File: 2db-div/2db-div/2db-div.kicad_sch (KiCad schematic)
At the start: 34 parts, among them J1001 Conn_01x02, J1002 From R2, J1003 Conn_01x02, J1004 Conn_Coaxial, SW1001 SW_SPDT, SW1002 Video, U1001 MC1458

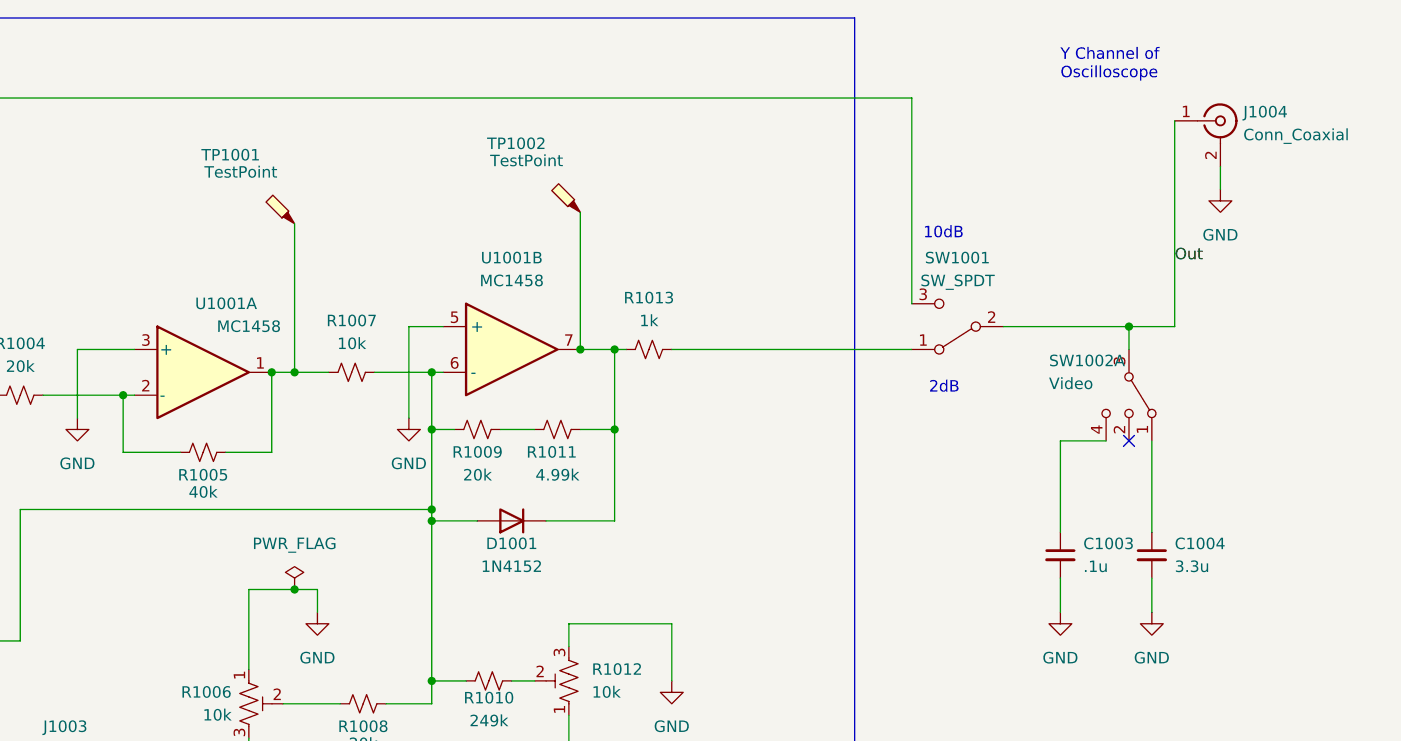
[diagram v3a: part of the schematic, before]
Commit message: BOM for 2db-div
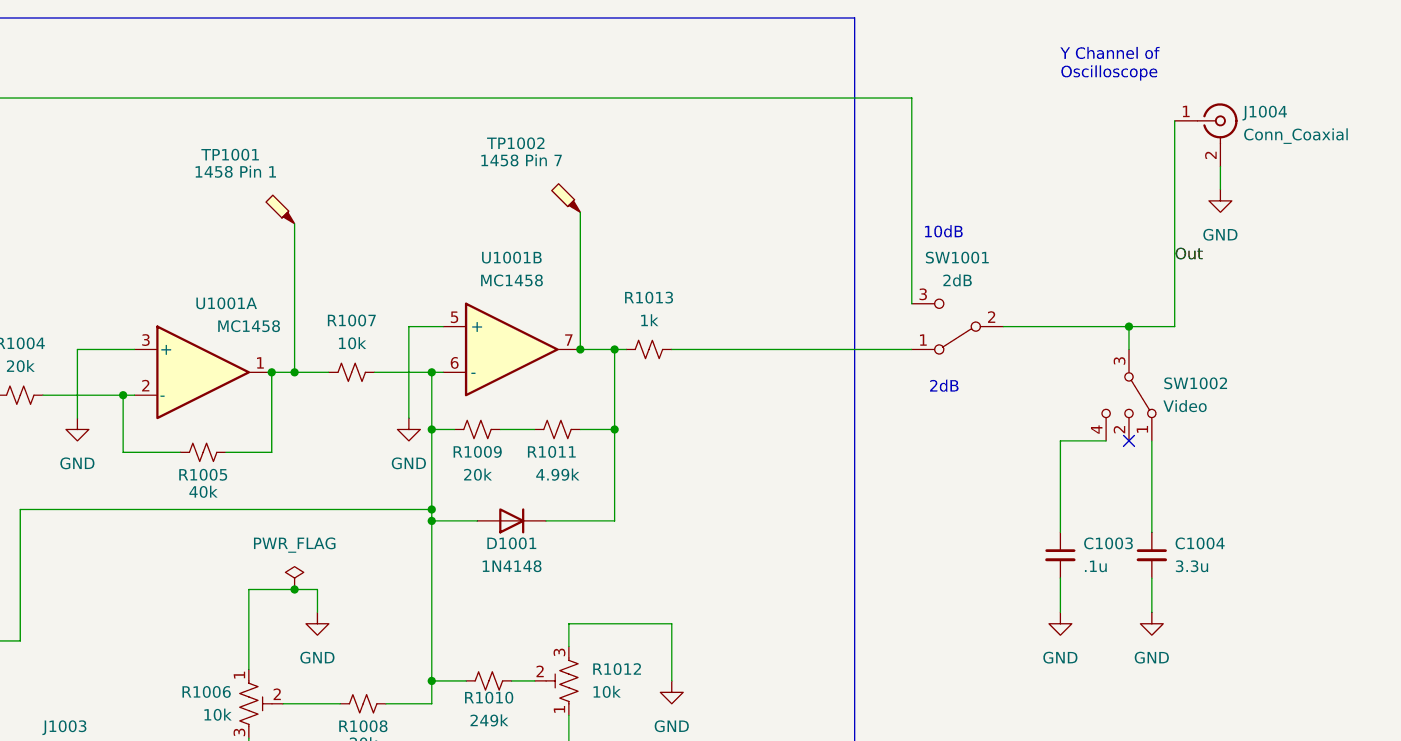
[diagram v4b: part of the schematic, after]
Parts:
- removed SW1002: Video, symbol Switch:SW_DP3T
- added SW1002: Video, symbol Switch:SW_SP3T
- D1001: value 1N4152 -> 1N4148
- SW1001: value SW_SPDT -> 2dB
- TP1001: value TestPoint -> 1458 Pin 1
- TP1002: value TestPoint -> 1458 Pin 7
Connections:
- net Out: now also SW1002.3
- net at C1004.1: now also SW1002.1
- net at C1003.1: now also SW1002.4
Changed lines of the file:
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@@
       (effects (font (size 1.27 1.27)) hide)
     )
-    (property "Datasheet" "" (id 3) (at 132.08 82.55 0))
+    (property "Datasheet" "https://www.ti.com/lit/ds/symlink/mc1458.pdf?HQS=dis-dk-null-digikeymode-dsf-pf-null-wwe&ts=1661113731735&ref_url=https%253A%252F%252Fwww.ti.com%252Fgeneral%252Fdocs%252Fsuppproductinfo.tsp%253FdistId%253D10%2526gotoUrl%253Dhttps%253A%252F%252Fwww.ti.com%252Flit%252Fgpn%252Fmc1458" (id 3) (at 132.08 82.55 0)
+      (effects (font (size 1.27 1.27)) hide)
+    )
     (property "Spice_Primitive" "X" (id 4) (at 132.08 82.55 0)
       (effects (font (size 1.27 1.27)) hide)
@@
     (pin "1")
   )
-  (symbol (lib_id "Switch:SW_DP3T") (at 227.33 85.09 270) (unit 1)
-    (in_bom yes) (on_board no)
-    (property "Reference" "SW1002" (id 0) (at 218.44 81.28 90)
-      (effects (font (size 1.27 1.27)) (justify left))
-    )
-    (property "Value" "Video" (id 1) (at 218.44 83.82 90)
+  (symbol (lib_id "power:GND") (at 49.53 193.04 0) (unit 1)
+    (in_bom yes) (on_board yes) (fields_autoplaced)
+    (property "Reference" "#PWR01002" (id 0) (at 49.53 199.39 0)
+      (effects (font (size 1.27 1.27)) hide)
+    )
+    (property "Value" "GND" (id 1) (at 49.53 198.12 0))
+    (property "Footprint" "" (id 2) (at 49.53 193.04 0)
+      (effects (font (size 1.27 1.27)) hide)
+    )
+    (property "Datasheet" "" (id 3) (at 49.53 193.04 0)
+      (effects (font (size 1.27 1.27)) hide)
+    )
+    (pin "1")
+  )
+  (symbol (lib_id "Switch:SW_SP3T") (at 227.33 85.09 270) (unit 1)
+    (in_bom yes) (on_board no) (fields_autoplaced)
+    (property "Reference" "SW1002" (id 0) (at 231.14 83.8199 90)
+      (effects (font (size 1.27 1.27)) (justify left))
+    )
+    (property "Value" "Video" (id 1) (at 231.14 86.3599 90)
       (effects (font (size 1.27 1.27)) (justify left))
     )
@@
     )
     (property "Datasheet" "~" (id 3) (at 231.775 69.215 0)
-      (effects (font (size 1.27 1.27)) hide)
-    )
-    (property "Spice_Primitive" "R" (id 4) (at 227.33 85.09 0)
-      (effects (font (size 1.27 1.27)) hide)
-    )
-    (property "Spice_Netlist_Enabled" "N" (id 5) (at 227.33 85.09 0)
       (effects (font (size 1.27 1.27)) hide)
     )
@@
     (pin "3")
     (pin "4")
-    (pin "5")
-    (pin "6")
-    (pin "7")
-    (pin "8")
-  )
-  (symbol (lib_id "power:GND") (at 49.53 193.04 0) (unit 1)
-    (in_bom yes) (on_board yes) (fields_autoplaced)
-    (property "Reference" "#PWR01002" (id 0) (at 49.53 199.39 0)
-      (effects (font (size 1.27 1.27)) hide)
-    )
-    (property "Value" "GND" (id 1) (at 49.53 198.12 0))
-    (property "Footprint" "" (id 2) (at 49.53 193.04 0)
-      (effects (font (size 1.27 1.27)) hide)
-    )
-    (property "Datasheet" "" (id 3) (at 49.53 193.04 0)
-      (effects (font (size 1.27 1.27)) hide)
-    )
-    (pin "1")
   )
   (symbol (lib_id "power:GND") (at 57.15 101.6 0) (unit 1)
@@
     (in_bom yes) (on_board no) (fields_autoplaced)
     (property "Reference" "SW1001" (id 0) (at 208.28 69.85 0))
-    (property "Value" "SW_SPDT" (id 1) (at 208.28 72.39 0))
+    (property "Value" "2dB" (id 1) (at 208.28 72.39 0))
     (property "Footprint" "" (id 2) (at 208.28 77.47 0)
       (effects (font (size 1.27 1.27)) hide)
@@
       (effects (font (size 1.27 1.27)) hide)
     )
-    (property "Datasheet" "~" (id 3) (at 78.74 123.19 0)
+    (property "Datasheet" "https://www.ti.com/lit/ds/symlink/mc1458.pdf?HQS=dis-dk-null-digikeymode-dsf-pf-null-wwe&ts=1661113731735&ref_url=https%253A%252F%252Fwww.ti.com%252Fgeneral%252Fdocs%252Fsuppproductinfo.tsp%253FdistId%253D10%2526gotoUrl%253Dhttps%253A%252F%252Fwww.ti.com%252Flit%252Fgpn%252Fmc1458" (id 3) (at 78.74 123.19 0)
       (effects (font (size 1.27 1.27)) hide)
     )
@@
       (effects (font (size 1.27 1.27)) (justify left))
     )
-    (property "Value" "TestPoint" (id 1) (at 164.465 59.055 0)
+    (property "Value" "1458 Pin 7" (id 1) (at 164.465 59.055 0)
       (effects (font (size 1.27 1.27)) (justify left))
     )
@@
       (effects (font (size 1.27 1.27)) (justify left))
     )
-    (property "Value" "TestPoint" (id 1) (at 132.715 60.325 0)
+    (property "Value" "1458 Pin 1" (id 1) (at 132.715 60.325 0)
       (effects (font (size 1.27 1.27)) (justify left))
     )
@@
     (in_bom yes) (on_board yes)
     (property "Reference" "D1001" (id 0) (at 158.75 101.6 0))
-    (property "Value" "1N4152" (id 1) (at 158.75 104.14 0))
+    (property "Value" "1N4148" (id 1) (at 158.75 104.14 0))
     (property "Footprint" "Diode_THT:D_DO-35_SOD27_P7.62mm_Horizontal" (id 2) (at 160.02 101.6 0)
       (effects (font (size 1.27 1.27)) hide)
@@
       (effects (font (size 1.27 1.27)) hide)
     )
-    (property "Datasheet" "~" (id 3) (at 158.75 80.01 0)
+    (property "Datasheet" "https://www.ti.com/lit/ds/symlink/mc1458.pdf?HQS=dis-dk-null-digikeymode-dsf-pf-null-wwe&ts=1661113731735&ref_url=https%253A%252F%252Fwww.ti.com%252Fgeneral%252Fdocs%252Fsuppproductinfo.tsp%253FdistId%253D10%2526gotoUrl%253Dhttps%253A%252F%252Fwww.ti.com%252Flit%252Fgpn%252Fmc1458" (id 3) (at 158.75 80.01 0)
       (effects (font (size 1.27 1.27)) hide)
     )
@@
     )
     (path "/d93477ae-5620-45e8-ad77-f7159e7b54ac"
-      (reference "D1001") (unit 1) (value "1N4152") (footprint "Diode_THT:D_DO-35_SOD27_P7.62mm_Horizontal")
+      (reference "D1001") (unit 1) (value "1N4148") (footprint "Diode_THT:D_DO-35_SOD27_P7.62mm_Horizontal")
     )
     (path "/39de73f6-b9de-4b63-8f42-aee5d12d3f40"
@@
     )
     (path "/7635f8f1-e32f-4bba-9fa7-adca3b4a9d43"
-      (reference "SW1001") (unit 1) (value "SW_SPDT") (footprint "")
-    )
-    (path "/1cab3287-f614-4c42-a22f-d78d04c3f6d0"
+      (reference "SW1001") (unit 1) (value "2dB") (footprint "")
+    )
+    (path "/268e017f-79dc-4e8c-ba2c-4bb52ba02a9d"
       (reference "SW1002") (unit 1) (value "Video") (footprint "")
     )
     (path "/b72f73df-8f47-4328-948e-122e87b26001"
-      (reference "TP1001") (unit 1) (value "TestPoint") (footprint "TestPoint:TestPoint_Pad_1.0x1.0mm")
+      (reference "TP1001") (unit 1) (value "1458 Pin 1") (footprint "TestPoint:TestPoint_Pad_1.0x1.0mm")
     )
     (path "/b1b40c84-9a02-4510-86b5-29948f09db79"
-      (reference "TP1002") (unit 1) (value "TestPoint") (footprint "TestPoint:TestPoint_Pad_1.0x1.0mm")
+      (reference "TP1002") (unit 1) (value "1458 Pin 7") (footprint "TestPoint:TestPoint_Pad_1.0x1.0mm")
     )
     (path "/15fa4751-8172-4686-95f4-602bee0fff9e"

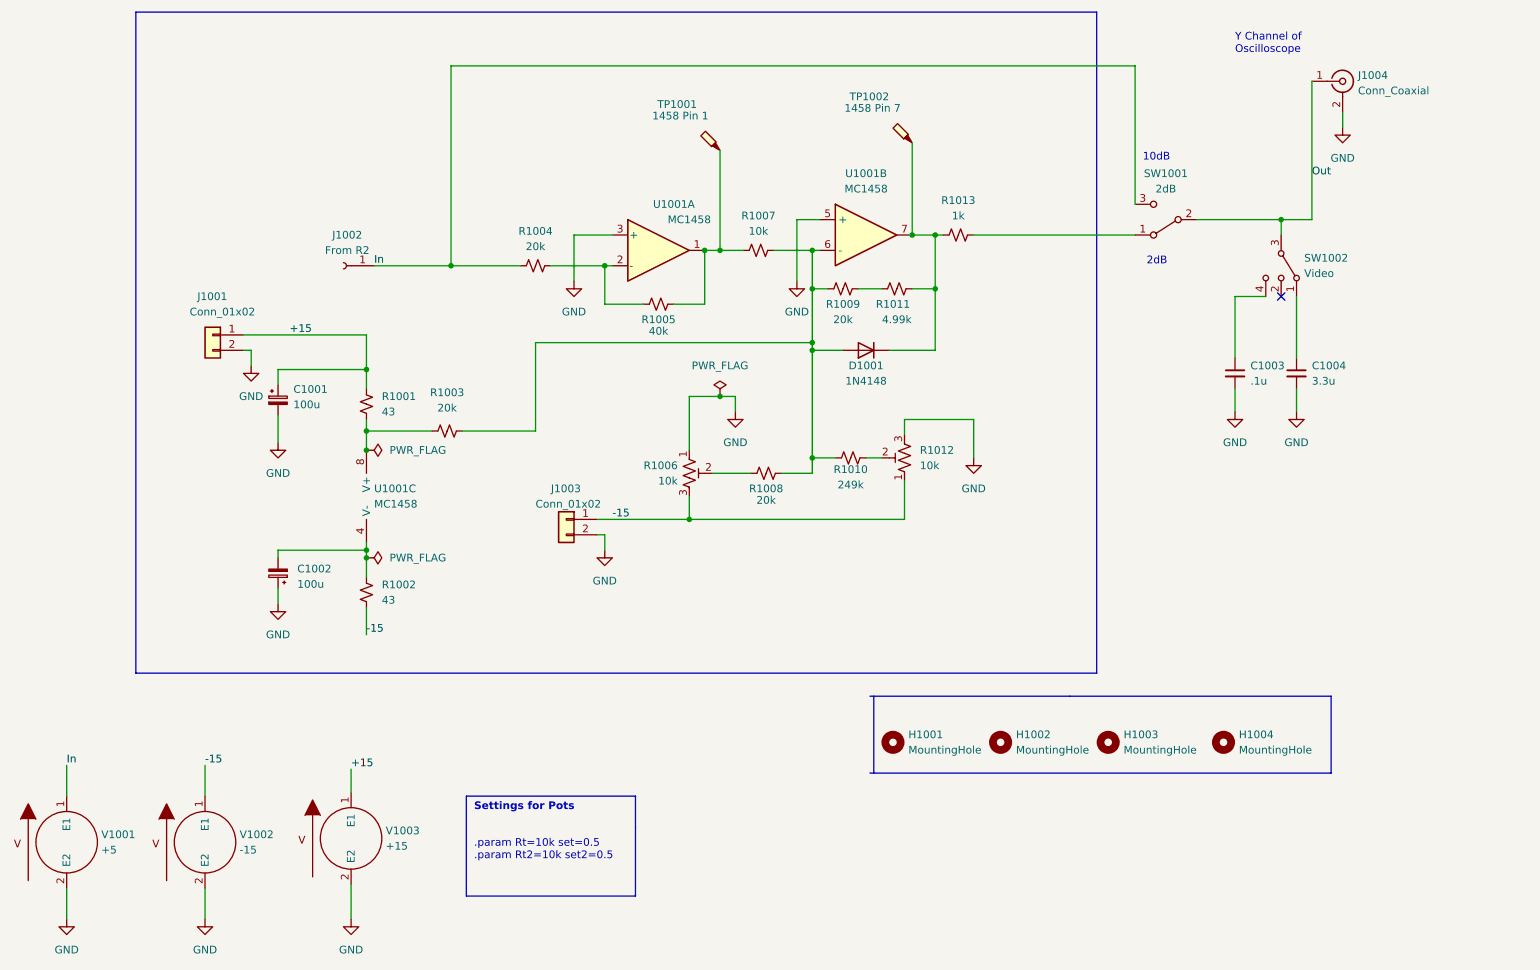
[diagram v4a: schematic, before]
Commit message: Hierarchical schematic updates
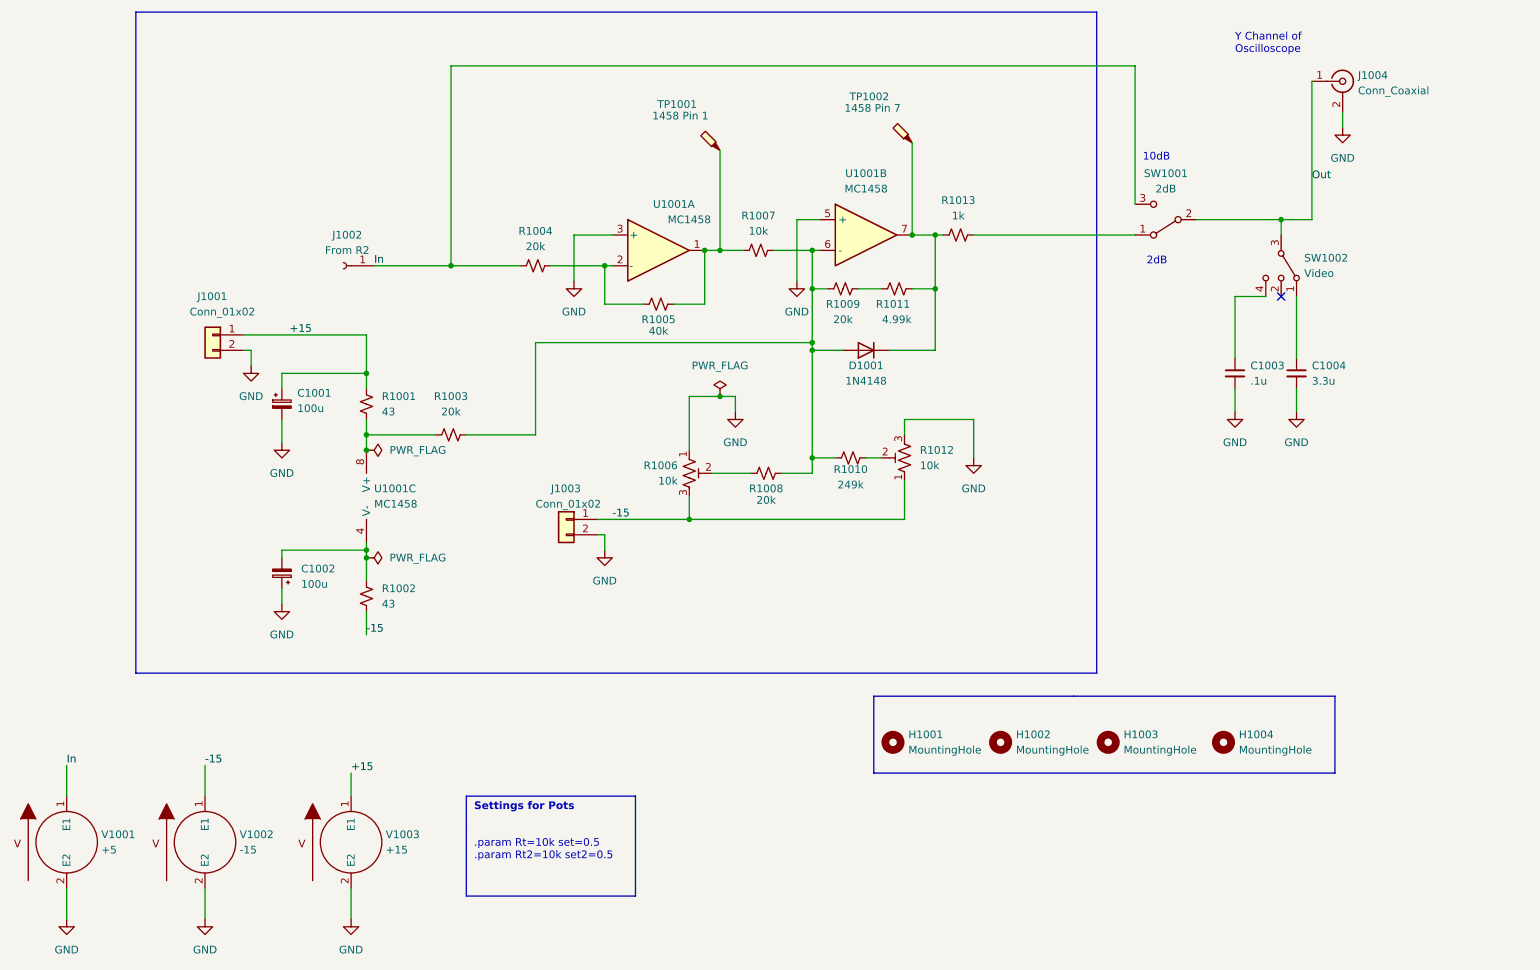
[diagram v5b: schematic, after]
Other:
- moved on the sheet: C1001, C1002, R1002, R1003, V1003

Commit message: minor changes for spice
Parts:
- H1001, H1002, H1003, H1004, SW1002: Spice_Netlist_Enabled (none) -> N; Spice_Primitive (none) -> R
- J1002: Spice_Model (none) -> From R2; Spice_Netlist_Enabled (none) -> N; Spice_Primitive (none) -> J
- SW1001: Spice_Model (none) -> 2dB
- U1001: Spice_Lib_File 2db-div-spice\MC1458-dual.lib -> 2db-div-spice\LM358-dual.lib; Spice_Model MC1458_ti -> LM358c; Spice_Netlist_Enabled Y -> N
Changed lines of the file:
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@@
+      (effects (font (size 1.27 1.27)) hide)
+    )
+    (property "Spice_Primitive" "R" (id 4) (at 180.975 163.83 0)
+      (effects (font (size 1.27 1.27)) hide)
+    )
+    (property "Spice_Netlist_Enabled" "N" (id 5) (at 180.975 163.83 0)
       (effects (font (size 1.27 1.27)) hide)
     )
@@
       (effects (font (size 1.27 1.27)) hide)
     )
-    (property "Spice_Model" "MC1458_ti" (id 5) (at 132.08 82.55 0)
-      (effects (font (size 1.27 1.27)) hide)
-    )
-    (property "Spice_Netlist_Enabled" "Y" (id 6) (at 132.08 82.55 0)
-      (effects (font (size 1.27 1.27)) hide)
-    )
-    (property "Spice_Lib_File" "2db-div-spice\\MC1458-dual.lib" (id 7) (at 132.08 82.55 0)
+    (property "Spice_Model" "LM358c" (id 5) (at 132.08 82.55 0)
+      (effects (font (size 1.27 1.27)) hide)
+    )
+    (property "Spice_Netlist_Enabled" "N" (id 6) (at 132.08 82.55 0)
+      (effects (font (size 1.27 1.27)) hide)
+    )
+    (property "Spice_Lib_File" "2db-div-spice\\LM358-dual.lib" (id 7) (at 132.08 82.55 0)
       (effects (font (size 1.27 1.27)) hide)
     )
@@
       (effects (font (size 1.27 1.27)) hide)
     )
+    (property "Spice_Primitive" "R" (id 4) (at 227.33 85.09 0)
+      (effects (font (size 1.27 1.27)) hide)
+    )
+    (property "Spice_Netlist_Enabled" "N" (id 5) (at 227.33 85.09 0)
+      (effects (font (size 1.27 1.27)) hide)
+    )
     (pin "1")
     (pin "2")
@@
       (effects (font (size 1.27 1.27)) hide)
     )
+    (property "Spice_Primitive" "R" (id 4) (at 217.805 163.83 0)
+      (effects (font (size 1.27 1.27)) hide)
+    )
+    (property "Spice_Netlist_Enabled" "N" (id 5) (at 217.805 163.83 0)
+      (effects (font (size 1.27 1.27)) hide)
+    )
   )
   (symbol (lib_id "Mechanical:MountingHole") (at 163.195 163.83 0) (unit 1)
@@
     )
     (property "Datasheet" "~" (id 3) (at 163.195 163.83 0)
+      (effects (font (size 1.27 1.27)) hide)
+    )
+    (property "Spice_Primitive" "R" (id 4) (at 163.195 163.83 0)
+      (effects (font (size 1.27 1.27)) hide)
+    )
+    (property "Spice_Netlist_Enabled" "N" (id 5) (at 163.195 163.83 0)
       (effects (font (size 1.27 1.27)) hide)
     )
@@
     )
     (property "Datasheet" "~" (id 3) (at 198.755 163.83 0)
+      (effects (font (size 1.27 1.27)) hide)
+    )
+    (property "Spice_Primitive" "R" (id 4) (at 198.755 163.83 0)
+      (effects (font (size 1.27 1.27)) hide)
+    )
+    (property "Spice_Netlist_Enabled" "N" (id 5) (at 198.755 163.83 0)
       (effects (font (size 1.27 1.27)) hide)
     )
@@
       (effects (font (size 1.27 1.27)) hide)
     )
+    (property "Spice_Model" "2dB" (id 6) (at 208.28 77.47 0)
+      (effects (font (size 1.27 1.27)) hide)
+    )
     (pin "1")
     (pin "2")
@@
       (effects (font (size 1.27 1.27)) hide)
     )
-    (property "Spice_Model" "MC1458_ti" (id 5) (at 155.575 80.01 0)
-      (effects (font (size 1.27 1.27)) hide)
-    )
-    (property "Spice_Netlist_Enabled" "Y" (id 6) (at 155.575 80.01 0)
-      (effects (font (size 1.27 1.27)) hide)
-    )
-    (property "Spice_Lib_File" "2db-div-spice\\MC1458-dual.lib" (id 7) (at 155.575 80.01 0)
+    (property "Spice_Model" "LM358c" (id 5) (at 155.575 80.01 0)
+      (effects (font (size 1.27 1.27)) hide)
+    )
+    (property "Spice_Netlist_Enabled" "N" (id 6) (at 155.575 80.01 0)
+      (effects (font (size 1.27 1.27)) hide)
+    )
+    (property "Spice_Lib_File" "2db-div-spice\\LM358-dual.lib" (id 7) (at 155.575 80.01 0)
       (effects (font (size 1.27 1.27)) hide)
     )
@@
       (effects (font (size 1.27 1.27)) hide)
     )
-    (property "Spice_Model" "MC1458_ti" (id 5) (at 158.75 80.01 0)
-      (effects (font (size 1.27 1.27)) hide)
-    )
-    (property "Spice_Netlist_Enabled" "Y" (id 6) (at 158.75 80.01 0)
-      (effects (font (size 1.27 1.27)) hide)
-    )
-    (property "Spice_Lib_File" "2db-div-spice\\MC1458-dual.lib" (id 7) (at 158.75 80.01 0)
+    (property "Spice_Model" "LM358c" (id 5) (at 158.75 80.01 0)
+      (effects (font (size 1.27 1.27)) hide)
+    )
+    (property "Spice_Netlist_Enabled" "N" (id 6) (at 158.75 80.01 0)
+      (effects (font (size 1.27 1.27)) hide)
+    )
+    (property "Spice_Lib_File" "2db-div-spice\\LM358-dual.lib" (id 7) (at 158.75 80.01 0)
       (effects (font (size 1.27 1.27)) hide)
     )
@@
       (effects (font (size 1.27 1.27)) hide)
     )
+    (property "Spice_Primitive" "J" (id 4) (at 72.39 85.09 0)
+      (effects (font (size 1.27 1.27)) hide)
+    )
+    (property "Spice_Model" "From R2" (id 5) (at 72.39 85.09 0)
+      (effects (font (size 1.27 1.27)) hide)
+    )
+    (property "Spice_Netlist_Enabled" "N" (id 6) (at 72.39 85.09 0)
+      (effects (font (size 1.27 1.27)) hide)
+    )
